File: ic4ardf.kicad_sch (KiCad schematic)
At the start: 26 parts, among them J1 Conn_Coaxial, J2 Barrel_Jack, SW1 SW_SPDT_312, U1 ATtiny85-20P, U2 Si5351module, U3 SA612, U4 LM386, U5 LM78L05_TO92, U6 L78L33_TO92

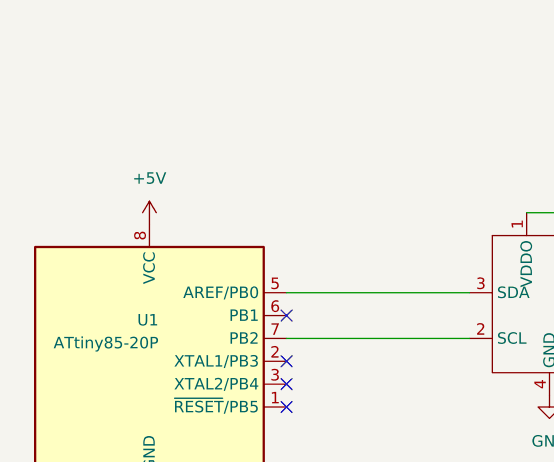
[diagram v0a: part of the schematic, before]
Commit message: fix attiny vcc +3v3 from +5v
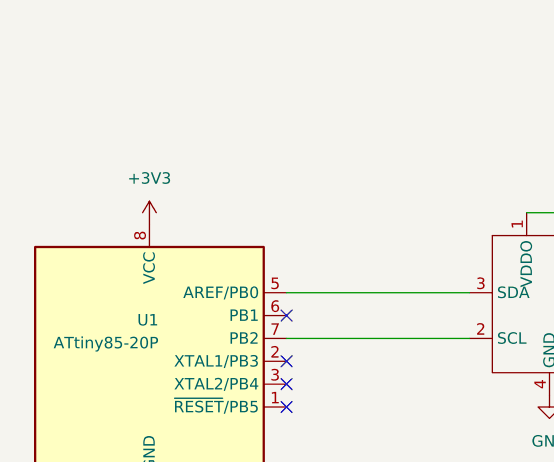
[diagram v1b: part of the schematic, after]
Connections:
- net +3V3: now also U1.8 (VCC)
- net +5V: no longer U1.8 (VCC)
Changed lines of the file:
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@@
+	)
+	(symbol
+		(lib_id "power:+3V3")
+		(at 74.93 66.04 0)
+		(unit 1)
+		(exclude_from_sim no)
+		(in_bom yes)
+		(on_board yes)
+		(dnp no)
+		(fields_autoplaced yes)
+		(property "Reference" "#PWR01"
+			(at 74.93 69.85 0)
+			(effects
+				(font
+					(size 1.27 1.27)
+				)
+				(hide yes)
+			)
+		)
+		(property "Value" "+3V3"
+			(at 74.93 60.96 0)
+			(effects
+				(font
+					(size 1.27 1.27)
+				)
+			)
+		)
+		(property "Footprint" ""
+			(at 74.93 66.04 0)
+			(effects
+				(font
+					(size 1.27 1.27)
+				)
+				(hide yes)
+			)
+		)
+		(property "Datasheet" ""
+			(at 74.93 66.04 0)
+			(effects
+				(font
+					(size 1.27 1.27)
+				)
+				(hide yes)
+			)
+		)
+		(property "Description" "Power symbol creates a global label with name \"+3V3\""
+			(at 74.93 66.04 0)
+			(effects
+				(font
+					(size 1.27 1.27)
+				)
+				(hide yes)
+			)
+		)
+		(pin "1"
+		)
+		(instances
+			(project "ic4ardf"
+				(path "/2e408510-bd2e-4630-85fb-49c607f33893"
+					(reference "#PWR01")
+					(unit 1)
+				)
+			)
+		)
 	)
 	(symbol
@@
 					(unit 1)
 				)
-			)
-		)
-	)
-	(symbol
-		(lib_id "power:+5V")
-		(at 74.93 66.04 0)
-		(unit 1)
-		(exclude_from_sim no)
-		(in_bom yes)
-		(on_board yes)
-		(dnp no)
-		(fields_autoplaced yes)
-		(property "Reference" "#PWR01"
-			(at 74.93 69.85 0)
-			(effects
-				(font
-					(size 1.27 1.27)
-				)
-				(hide yes)
-			)
-		)
-		(property "Value" "+5V"
-			(at 74.93 60.96 0)
-			(effects
-				(font
-					(size 1.27 1.27)
-				)
-			)
-		)
-		(property "Footprint" ""
-			(at 74.93 66.04 0)
-			(effects
-				(font
-					(size 1.27 1.27)
-				)
-				(hide yes)
-			)
-		)
-		(property "Datasheet" ""
-			(at 74.93 66.04 0)
-			(effects
-				(font
-					(size 1.27 1.27)
-				)
-				(hide yes)
-			)
-		)
-		(property "Description" "Power symbol creates a global label with name \"+5V\""
-			(at 74.93 66.04 0)
-			(effects
-				(font
-					(size 1.27 1.27)
-				)
-				(hide yes)
-			)
-		)
-		(pin "1"
-		)
-		(instances
-			(project "ic4ardf"
-				(path "/2e408510-bd2e-4630-85fb-49c607f33893"
-					(reference "#PWR01")
-					(unit 1)
-				)
